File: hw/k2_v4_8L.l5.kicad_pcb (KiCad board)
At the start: 8 copper layers, 120 x 46 mm, 59 parts, among them J11 J_EC_HEADER, J12 J_12V_IN, J13 J_SWD, J2 SlimSAS_x8_SFF8654, J3 MCIO_4i_SFF1016, J4 MCIO_4i_SFF1016, J6 J_PWR_CTRL, J9 J_OOB_HEADER, U1 STM32G0B1CBT6, U2 DCDC_12V_3V3, U4 BAT54C, U5 OPTO_LTV356T, U6 DS320PR1601

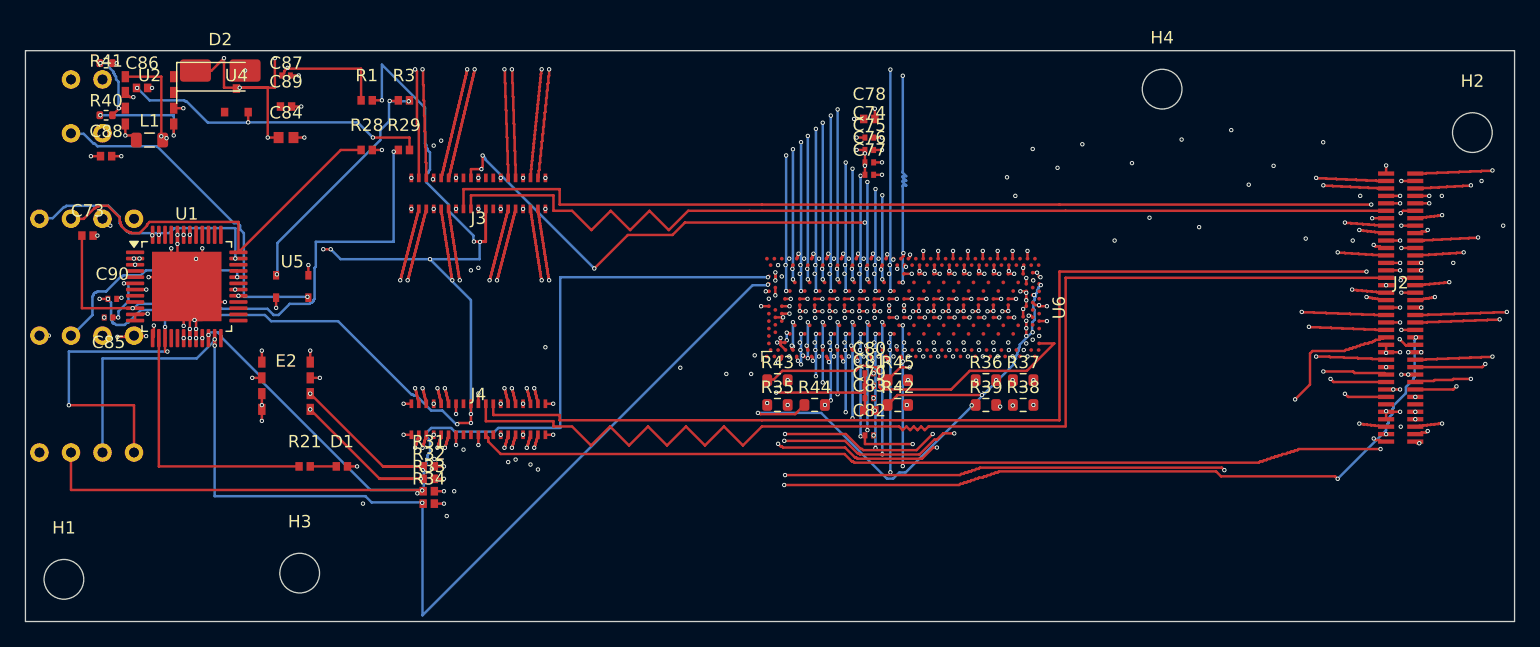
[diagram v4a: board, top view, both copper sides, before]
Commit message: p4(k2): #K2-23 §二-12 落件提交 —— 五步复合板 6ff49da5678c2108 + project.yaml 9cee872bd6fbdc67 + SPEC rev-47 9ba09cbc148d6836（可追溯性缺口收口）
依据：#K2-21 §二①（落件批准，带条件）· #K2-23 §二-12（令提交）· 宪法第三条（可追溯 commit hash）。
现象：P4 唯一落件板 + project.yaml + SPEC rev-47 仅存工作树 32 轮，`git checkout` 即回退。

条件闭合（#K2-21 §二① 四条）
1. 落件器 v2 `k2_p4_composed_land_v2.py` f702bf8be289358d，以 `--silk-report <台账> --apply --confirm-repo-write`（T-41 双旗标）落库。
2. dst pro 逐字节不变：落件时 = f68a5fb2f82bd02d（沙箱端到端实证见 K2-P4-SILK-TEXT-RESIDUAL-FIX-v1.md §4）。
   其后 f68a5fb2→d5e0ca067a7b585e 系 #K2-21 §二③「9 条 ignore 朝严摘除」授权动作，已于 a2e4f1d 单独提交；本笔 pro 干净、未夹带。
3. 复跑 + 逐段 sha（本笔实测）：
   - hw/k2_v4_8L.l5.kicad_pcb          6ff49da5678c2108（= 批准值）
   - pm_gate/project.yaml              9cee872bd6fbdc67（= 批准值）
   - SPEC_k2_v4.spec-rev-47.json       9ba09cbc148d6836（= 批准值）
   - hw/k2_v4_8L.l5.kicad_pro          d5e0ca067a7b585e（未动）
4. 冻结判定器（criteria/adjudicate.py 897e8bfde60e2cfe + manifest.k2.yaml 7ce08757eff25557，board l5 + errata-1 + sch-dir）：
   PASS 7 / FAIL 3（PROVISIONAL，manifest 未签认）
   PASS = device_has_pads · drill_count(NPTH=4/PTH=16) · non45_segments 0/4721 · rule_severity_manifest(ignore 0/62) · net_declared_realized · pin_map_complete · verdict_schema
   FAIL = zone_filled 10/18 · refdes_sets_equal(图 55/板 59；板有图无 4) · pipeline_present(hw/sch)
   DRC（同名 pro，severity-all）：75 违反全为 warning（missing_courtyard 40 + lib_footprint_mismatch 35）· error 0 · unconnected 0 · footprint errors 0

未夹带：无任何判据/severity/口径变更（criteria/**、_shared/**、pro 未动）；未含 hw/k2_v4_8L.l5.kicad_prl（KiCad 本地 UI 态，非 P4 证据件；4 份历史 .prl 入库系早期遗留，不循）。
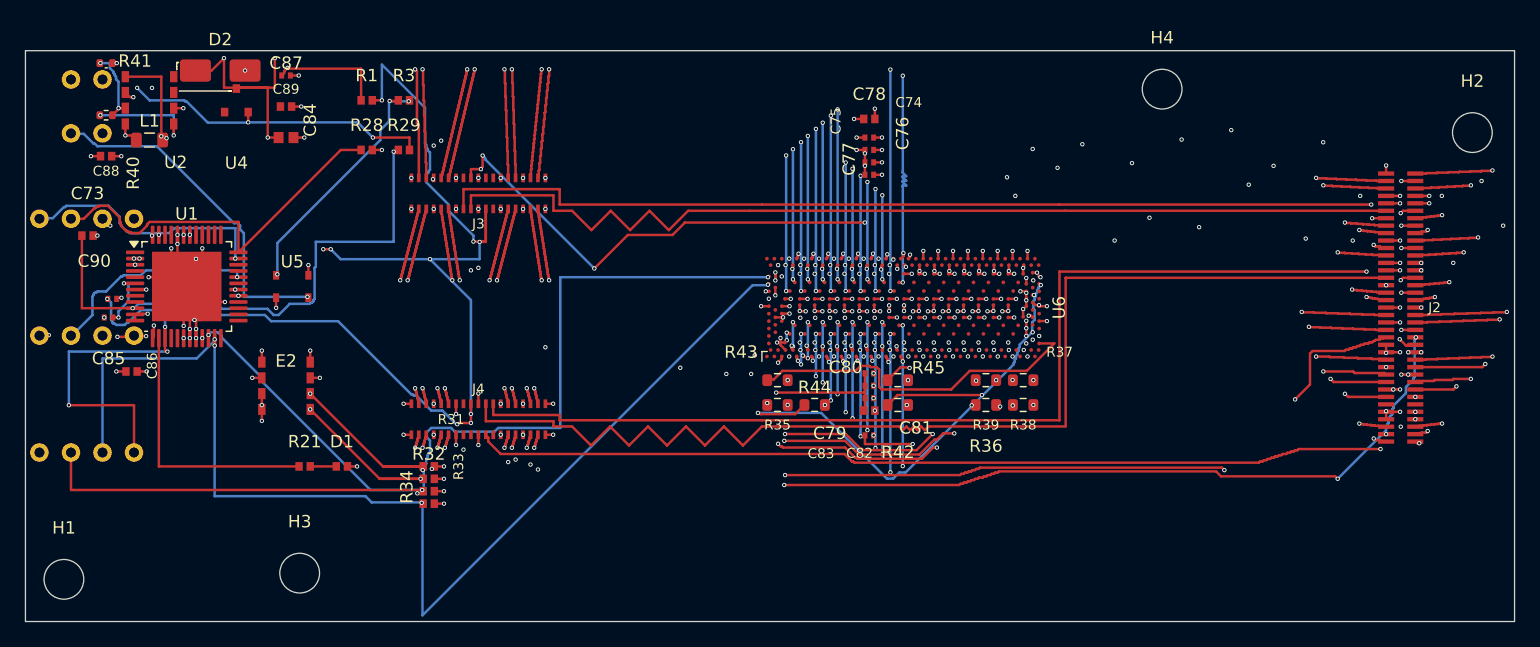
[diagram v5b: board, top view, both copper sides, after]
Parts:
- moved C86 22.9 mm to (31.6, 58.9)
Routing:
- net P3V3_AUX: track 118.6 -> 121.2 mm, vias 14 -> 13
- net MCU_VDD: track 36.6 -> 37.3 mm, vias 18 -> 15
- net I2C2_SCL: track 100.9 -> 100.2 mm
- net P3V3: track 61.0 -> 61.5 mm, vias 45 -> 44
- net GND: track 95.0 -> 95.5 mm, vias 312 -> 313

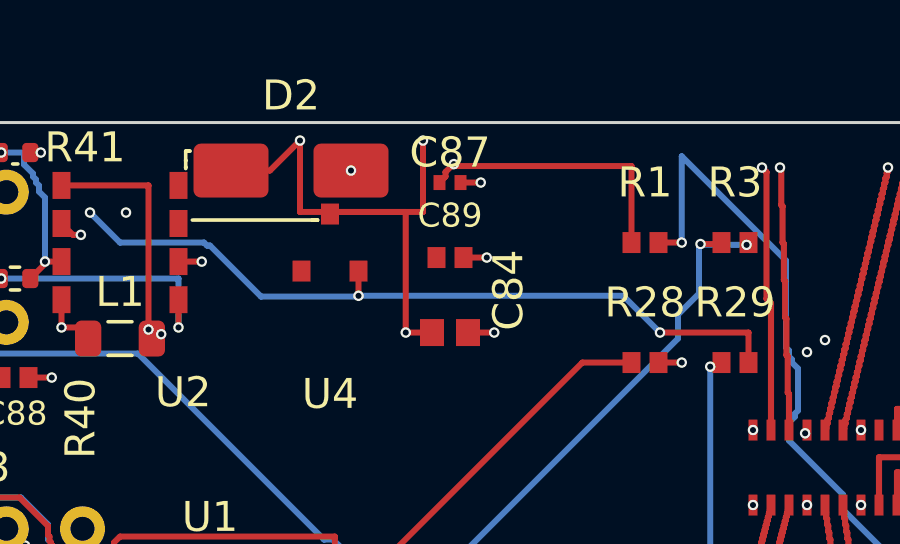
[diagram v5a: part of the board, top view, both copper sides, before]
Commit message: p4(k2): owner ⑤ 执行（#K2-24）—— 删 C89 + PWR_5V_KEY，7 载体一次做净
真源 bump（新件 errata-2 61c4694e：nets 101→100 / GND 211→210 / placements 55→54；原件 dd794c54 不动）
SPEC bump rev-50 ed0950687e5aec97（深 diff 断言：low_speed_nets 19→18 · power_pad_connect.entries 185→184
  · live board_sha16×3+basis（6ff49da5→dae8dc8d）· 新增 _spec_rev_50；retired_superseded_* 两条按红线留存）
pro 35c8f34bde7ac00c（netclass_assignments 146→145，文本级 3 行）· BOM db081546bbe64c37（54 refs）
受审板 l5 6ff49da5678c2108→dae8dc8d48ff5b81（删 C89 fps59→58 + GND 短段 + 端点缝合 via + 孤网 PWR_5V_KEY）
原理图 1 件 cb3c2134→dbaa989e（其余 5 件逐字节同；符号库未变）· project.yaml 56583331599fab0f（spec_name rev-50 / nets_yaml errata-2）
图集 v11 e284e9afd9054408（55→54 件；01/02/05 变，03/04/06/07 未漂）· 落位解逐字节不变（C89 不在 15 件解内，具名）

守恒闸：未连接 0 · DRC 类型集不增（73=39courtyard+34lib_mismatch；沙箱 lib_footprint_issues 已由同址对照臂证为位置伪差）
  · 非 45° 0/4720 · 阻抗/等长/走廊不退化（SPEC 深 diff + 图集 C4/C6/D1 pass + refplane 逐值同前）· 冻结四源不变
判定器：PASS 7 / FAIL 3（集合同名；net_declared_realized「<2 焊盘」1→0；refdes 55/59→54/58）
⚠️ 生成器一项未达（具名上报，未改）：k2_gen_v5.py 的 K2_REFS 取自冻结锚板（:54/:68-77/:79，断言 :830-835）⇒
  ❌ 写盘阻断 [YAML] ... 不存在 ref: ['C89']；最小补丁提案（K2_REFS 改读真源 YAML）须监理批
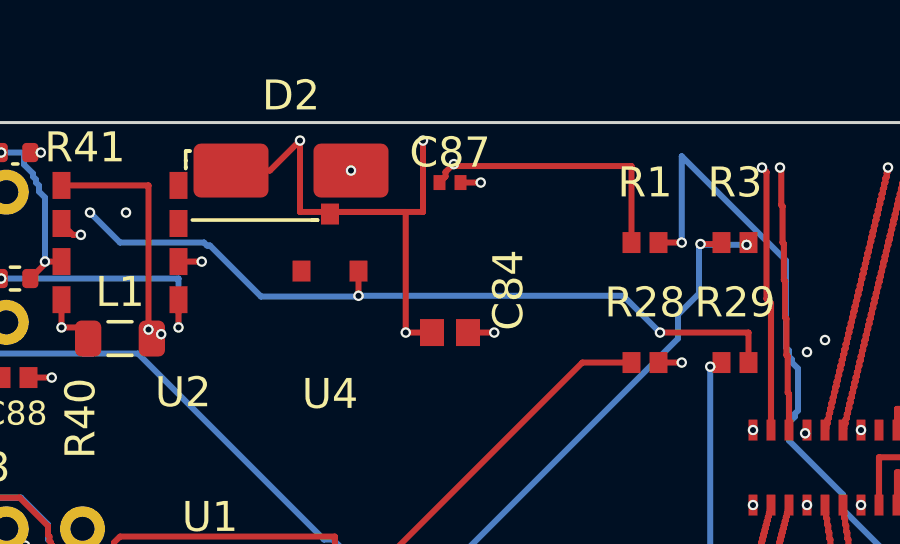
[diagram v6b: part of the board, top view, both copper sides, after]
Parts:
- removed C89: 4.7uF, Capacitor_SMD:C_0603_1608Metric
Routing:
- net GND: track 95.5 -> 94.7 mm, vias 313 -> 312
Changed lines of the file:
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@@
 		)
 	)
-	(footprint "Capacitor_SMD:C_0603_1608Metric"
-		(layer "F.Cu")
-		(at 44 37.5)
-		(property "Reference" "C89"
-			(at 0 -1.4 0)
-			(layer "F.SilkS")
-			(effects
-				(font
-					(size 0.8 0.8)
-					(thickness 0.12)
-				)
-			)
-		)
-		(property "Value" "4.7uF"
-			(at 0 2 0)
-			(layer "F.Fab")
-			(effects
-				(font
-					(size 1 1)
-					(thickness 0.15)
-				)
-			)
-		)
-		(property "Datasheet" ""
-			(at 0 0 0)
-			(layer "F.Fab")
-			(hide yes)
-			(effects
-				(font
-					(size 1.27 1.27)
-				)
-			)
-		)
-		(property "Description" ""
-			(at 0 0 0)
-			(layer "F.Fab")
-			(hide yes)
-			(effects
-				(font
-					(size 1.27 1.27)
-				)
-			)
-		)
-		(duplicate_pad_numbers_are_jumpers no)
-		(pad "1" smd rect
-			(at -0.45 0)
-			(size 0.6 0.7)
-			(layers "F.Cu" "F.Mask" "F.Paste")
-			(net "PWR_5V_KEY")
-		)
-		(pad "2" smd rect
-			(at 0.45 0)
-			(size 0.6 0.7)
-			(layers "F.Cu" "F.Mask" "F.Paste")
-			(net "GND")
-		)
-		(embedded_fonts no)
-	)
 	(footprint "R_0603_1608Metric"
 		(layer "F.Cu")
@@
 	)
 	(segment
-		(start 44.45 37.5)
-		(end 45.225 37.5)
-		(width 0.2)
-		(layer "F.Cu")
-		(net "GND")
-	)
-	(segment
 		(start 28.45 47.9)
 		(end 28.8 47.9)
@@
 		(size 0.35)
 		(drill 0.2)
-		(layers "F.Cu" "B.Cu")
-		(net "GND")
-	)
-	(via
-		(at 45.225 37.5)
-		(size 0.35)
-		(drill 0.2)
